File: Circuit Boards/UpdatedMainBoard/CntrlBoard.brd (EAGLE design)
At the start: 101.6 x 81.3 mm, 49 parts, among them P1 22-23-2021, P10 3PIN2MMPITCH, P11 3PIN2MMPITCH, P12 DF3A-2P-2DSA, P13 DF3A-2P-2DSA, P14 DF3A-2P-2DSA, P15 DF3A-2P-2DSA, P16 DF3A-2P-2DSA, P17 DF3A-2P-2DSA, P18 DF3A-2P-2DSA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

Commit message: Control Board update finished
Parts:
- added R13: 100R, resistor:R1206
- added R14: 300R, resistor:R1206
- added U$3: RSHUNT, resistor:CM2512SHUNT
- added U$4: LT6106, linear-technology:TSOT23-6
- P10, P11, P7, P8, P9: value 3PIN2MMPITCH -> 3MM2MMLOCKING; device con-3m:3PIN_2MMPITCH -> con-3m:3PIN_2MMLOCKING
- moved LED3 94.6 mm to (98.4, 18.4), turned to 0 degrees
- moved P7 14.7 mm to (51.4, 14.0)
- moved P8 10.9 mm to (57.8, 14.0)
- moved U$1 8.91 mm to (61.0, 4.45)
- moved R9 8.26 mm to (3.81, 73.0), turned to 90 degrees
- moved P9 7.10 mm to (64.1, 14.0)
- moved R8 6.38 mm to (3.17, 66.0)
- moved P14 6.35 mm to (6.35, 50.8)
- moved LED4 4.49 mm to (12.1, 66.7)
- moved P16 4.45 mm to (6.35, 45.1)
- moved P2 3.81 mm to (8.89, 15.2)
- moved P10 3.42 mm to (70.5, 14.0)
- moved P12 3.17 mm to (14.0, 42.5)
- moved P13 2.54 mm to (14.0, 50.8)
- moved P15 2.54 mm to (6.35, 39.4)
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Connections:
- new net N$22: SW1.1, U$3.I2
- new net N$24: R13.1, U$3.E2
- new net N$25: R13.2, U$4.3
- new net N$26: U$3.E1, U$4.4
- new net V_CURRENT: R14.1, U$4.1, U1.A7
- net GND: now also R14.2, U$4.2
- net VCC: now also U$3.I1, U$4.6; no longer SW1.1
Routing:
- net N$12: track 7.01 -> 144.8 mm, vias 1 -> 3
- net VCC: track 175.4 -> 240.4 mm, vias 5 -> 8
- net N$25: track 0.00 -> 54.2 mm, vias 0 -> 1
- net GND: track 454.3 -> 488.3 mm, vias 5 -> 7
- net N$26: track 0.00 -> 32.2 mm, vias 0 -> 1
- net V_CURRENT: track 0.00 -> 26.2 mm
- net N$22: track 0.00 -> 17.9 mm
- net +5V: track 191.9 -> 208.4 mm
- net TANK_LEVEL: track 14.5 -> 27.8 mm
- net N$27: track 28.2 -> 37.9 mm
- net N$1: track 67.2 -> 57.7 mm
- net LIN_POS: track 14.5 -> 24.0 mm
- net N$24: track 0.00 -> 9.12 mm
- net ROT_POS: track 14.5 -> 20.2 mm
- net N$10: track 8.26 -> 11.4 mm
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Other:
- outline, holes or cut-outs redrawn
- board text added: "24V"
- board text added: "24V IN"
- board text added: "24V OUT"
- board text added: "24V OUTS"
- board text added: "5V"
- board text added: "5V ENABLE"
- board text added: "5V OUT"
- board text added: "5V OUTS"
- board text added: "IMU SERIAL"
- board text added: "LINEAR"
- board text added: "PUMP DIR."
- board text added: "PUMP DIRECTION"
- board text added: "PUMP ON"
- board text added: "ROTARY"

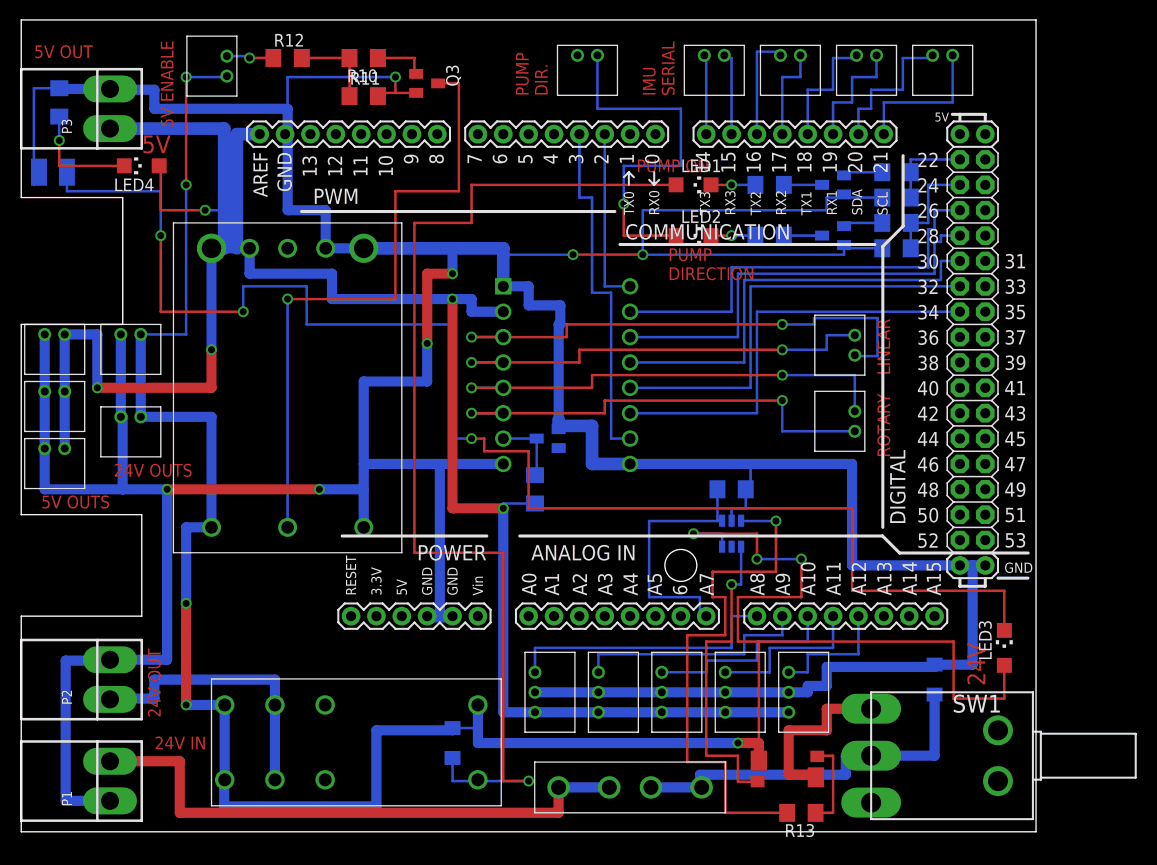
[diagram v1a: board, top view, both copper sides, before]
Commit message: Added 6 pin connector
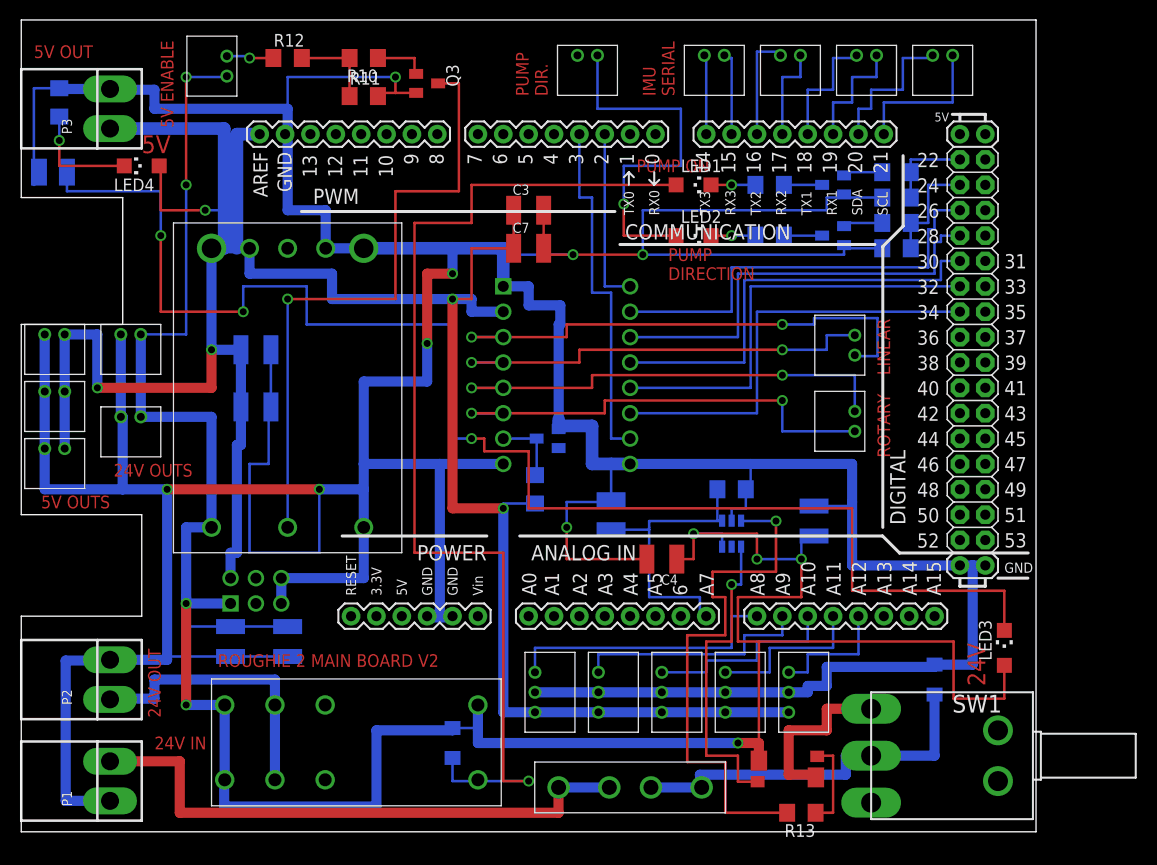
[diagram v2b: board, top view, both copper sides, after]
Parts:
- added C1, C2, C3, C4: 10U, resistor:C1210K
- added C5, C6, C7, C8, C9: 0U1, resistor:C1210K
- added P22: 6PIN2ROWARDUINO, con-3m:6PIN2ROWARDUINO
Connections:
- net +5V: now also C1.1, C3.1, C6.1, C7.1, P22.P$2
- net GND: now also C1.2, C2.2, C3.2, C4.2, C5.2, C6.2, C7.2, C8.2, C9.2, P22.P$5, P22.P$6
- net VCC: now also C2.1, C4.1, C5.1, C8.1, P22.P$1
- net V_CURRENT: now also C9.1
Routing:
- net GND: track 488.3 -> 585.7 mm, vias 7 -> 8
- net +5V: track 208.4 -> 250.3 mm
- net VCC: track 240.4 -> 265.4 mm
- net V_CURRENT: track 26.2 -> 30.0 mm
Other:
- board text added: "ROUGHIE 2 MAIN BOARD V2"
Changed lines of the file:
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@@
 DIR.</text>
 <text x="15.24" y="70.485" size="1.27" layer="1" font="vector" rot="R90">5V ENABLE</text>
+<text x="19.685" y="16.51" size="1.27" layer="1" font="vector">ROUGHIE 2 MAIN BOARD V2</text>
 </plain>
 <attributes>
@@
 <element name="U$4" library="linear-technology" package="TSOT23-6" value="LT6106" x="71.12" y="29.845" rot="MR180"/>
 <element name="R14" library="resistor" package="R1206" value="300R" x="71.12" y="34.29" rot="MR180"/>
+<element name="C1" library="resistor" package="C1210K" value="10U" x="23.495" y="48.26" rot="MR180"/>
+<element name="C2" library="resistor" package="C1210K" value="10U" x="20.955" y="19.05" rot="MR270"/>
+<element name="C3" library="resistor" package="C1210K" value="10U" x="50.8" y="62.23"/>
+<element name="C4" library="resistor" package="C1210K" value="10U" x="64.135" y="27.305" rot="R180"/>
+<element name="C5" library="resistor" package="C1210K" value="0U1" x="26.67" y="19.05" rot="MR270"/>
+<element name="C6" library="resistor" package="C1210K" value="0U1" x="23.495" y="42.545" rot="MR180"/>
+<element name="C7" library="resistor" package="C1210K" value="0U1" x="50.8" y="58.42"/>
+<element name="C8" library="resistor" package="C1210K" value="0U1" x="79.375" y="31.115" rot="MR90"/>
+<element name="C9" library="resistor" package="C1210K" value="0U1" x="59.055" y="31.75" rot="MR90"/>
+<element name="P22" library="con-3m" package="6PIN2ROWARDUINO" value="6PIN2ROWARDUINO" x="20.955" y="22.86"/>
 </elements>
 <signals>
@@
 <wire x1="60.96" y1="36.83" x2="73.025" y2="36.83" width="1.016" layer="16"/>
 <wire x1="73.025" y1="36.83" x2="83.185" y2="36.83" width="1.016" layer="16"/>
-<wire x1="83.185" y1="36.83" x2="83.185" y2="26.67" width="1.016" layer="16"/>
+<wire x1="83.185" y1="36.83" x2="83.185" y2="33.02" width="1.016" layer="16"/>
+<wire x1="83.185" y1="33.02" x2="83.185" y2="26.67" width="1.016" layer="16"/>
 <wire x1="83.185" y1="26.67" x2="93.98" y2="26.67" width="1.016" layer="16"/>
 <wire x1="48.26" y1="54.61" x2="50.8" y2="54.61" width="1.016" layer="16"/>
@@
 <wire x1="40.64" y1="21.59" x2="41.91" y2="21.59" width="1.016" layer="16"/>
 <wire x1="41.91" y1="21.59" x2="41.91" y2="36.83" width="1.016" layer="16"/>
-<wire x1="60.96" y1="36.83" x2="57.15" y2="36.83" width="1.27" layer="16"/>
+<wire x1="60.96" y1="36.83" x2="59.055" y2="36.83" width="1.27" layer="16"/>
+<wire x1="59.055" y1="36.83" x2="57.15" y2="36.83" width="1.27" layer="16"/>
 <wire x1="57.15" y1="36.83" x2="57.15" y2="40.64" width="1.27" layer="16"/>
 <wire x1="57.15" y1="40.64" x2="53.805" y2="40.64" width="1.27" layer="16"/>
@@
 <wire x1="2.350009375" y1="34.29" x2="2.350009375" y2="38.369240625" width="1.016" layer="16"/>
 <wire x1="9.970009375" y1="49.799240625" x2="9.970009375" y2="41.544240625" width="1.016" layer="16"/>
-<wire x1="14.605" y1="17.2212" x2="14.605" y2="34.29" width="1.016" layer="16"/>
+<wire x1="14.605" y1="17.2212" x2="14.605" y2="17.55" width="1.016" layer="16"/>
 <via x="14.605" y="34.29" extent="1-16" drill="0.7" shape="square"/>
+<wire x1="14.605" y1="17.55" x2="14.605" y2="34.29" width="1.016" layer="16"/>
 <wire x1="14.605" y1="34.29" x2="29.845" y2="34.29" width="1.016" layer="1"/>
 <via x="29.845" y="34.29" extent="1-16" drill="0.7" shape="square"/>
@@
 <wire x1="71.12" y1="32.385" x2="72.542" y2="32.385" width="0.254" layer="16"/>
 <wire x1="72.542" y1="32.385" x2="72.542" y2="34.29" width="0.254" layer="16"/>
+<contactref element="C4" pad="2"/>
+<contactref element="C8" pad="2"/>
+<contactref element="C9" pad="2"/>
+<contactref element="C3" pad="2"/>
+<contactref element="C7" pad="2"/>
+<contactref element="C2" pad="2"/>
+<contactref element="C5" pad="2"/>
+<contactref element="C1" pad="2"/>
+<contactref element="C6" pad="2"/>
+<wire x1="59.055" y1="33.25" x2="59.055" y2="36.83" width="0.254" layer="16"/>
+<wire x1="62.635" y1="27.305" x2="54.61" y2="27.305" width="0.254" layer="1"/>
+<wire x1="54.61" y1="27.305" x2="54.61" y2="30.48" width="0.254" layer="1"/>
+<via x="54.61" y="30.48" extent="1-16" drill="0.7" shape="square"/>
+<wire x1="54.61" y1="30.48" x2="54.61" y2="33.02" width="0.254" layer="16"/>
+<wire x1="54.61" y1="33.02" x2="59.055" y2="33.02" width="0.254" layer="16"/>
+<wire x1="59.055" y1="33.02" x2="59.055" y2="33.25" width="0.254" layer="16"/>
+<wire x1="79.375" y1="32.615" x2="83.185" y2="32.615" width="0.254" layer="16"/>
+<wire x1="83.185" y1="32.615" x2="83.185" y2="33.02" width="0.254" layer="16"/>
+<wire x1="52.3" y1="62.23" x2="52.3" y2="58.42" width="0.254" layer="1"/>
+<wire x1="52.3" y1="58.42" x2="52.705" y2="58.42" width="0.254" layer="1"/>
+<wire x1="52.705" y1="58.42" x2="52.705" y2="57.785" width="0.254" layer="1"/>
+<wire x1="52.705" y1="57.785" x2="55.245" y2="57.785" width="0.254" layer="1"/>
+<wire x1="24.995" y1="48.26" x2="24.995" y2="42.545" width="0.254" layer="16"/>
+<wire x1="24.995" y1="42.545" x2="24.765" y2="42.545" width="0.254" layer="16"/>
+<wire x1="24.765" y1="42.545" x2="24.765" y2="36.83" width="0.254" layer="16"/>
+<wire x1="24.765" y1="36.83" x2="22.86" y2="36.83" width="0.254" layer="16"/>
+<wire x1="22.86" y1="36.83" x2="22.86" y2="27.94" width="0.254" layer="16"/>
+<wire x1="22.86" y1="27.94" x2="29.845" y2="27.94" width="0.254" layer="16"/>
+<wire x1="29.845" y1="27.94" x2="29.845" y2="34.29" width="0.254" layer="16"/>
+<wire x1="26.67" y1="17.55" x2="20.955" y2="17.55" width="0.254" layer="16"/>
+<wire x1="20.955" y1="17.55" x2="14.605" y2="17.55" width="0.254" layer="16"/>
+<contactref element="P22" pad="P$6"/>
+<contactref element="P22" pad="P$5"/>
+<wire x1="26.035" y1="22.86" x2="26.035" y2="25.4" width="1.016" layer="16"/>
+<wire x1="26.035" y1="25.4" x2="34.29" y2="25.4" width="1.016" layer="16"/>
+<wire x1="34.29" y1="25.4" x2="34.29" y2="30.48" width="1.016" layer="16"/>
 </signal>
 <signal name="N$1">
@@
 <wire x1="45.72" y1="10.3886" x2="45.72" y2="10.16" width="0.254" layer="16"/>
 <wire x1="19.05" y1="30.48" x2="16.51" y2="30.48" width="1.016" layer="16"/>
-<wire x1="16.51" y1="30.48" x2="16.51" y2="22.86" width="1.016" layer="16"/>
+<wire x1="16.51" y1="30.48" x2="16.51" y2="23.495" width="1.016" layer="16"/>
 <via x="16.51" y="22.86" extent="1-16" drill="0.7" shape="square"/>
+<wire x1="16.51" y1="23.495" x2="16.51" y2="22.86" width="1.016" layer="16"/>
 <wire x1="16.51" y1="22.86" x2="16.51" y2="12.7" width="1.016" layer="1"/>
 <via x="16.51" y="12.7" extent="1-16" drill="0.7" shape="square"/>
@@
 <wire x1="67.31" y1="29.845" x2="70.17" y2="29.845" width="0.254" layer="16"/>
 <wire x1="70.17" y1="29.845" x2="70.17" y2="28.545" width="0.254" layer="16"/>
+<contactref element="C4" pad="1"/>
+<contactref element="C8" pad="1"/>
+<contactref element="C5" pad="1"/>
+<contactref element="C2" pad="1"/>
+<wire x1="65.635" y1="27.305" x2="67.31" y2="27.305" width="0.254" layer="1"/>
+<wire x1="67.31" y1="27.305" x2="67.31" y2="29.845" width="0.254" layer="1"/>
+<wire x1="79.375" y1="29.615" x2="78.105" y2="29.615" width="0.254" layer="16"/>
+<wire x1="78.105" y1="29.615" x2="78.105" y2="27.305" width="0.254" layer="16"/>
+<wire x1="26.67" y1="20.55" x2="20.955" y2="20.55" width="0.254" layer="16"/>
+<wire x1="16.51" y1="23.725" x2="16.51" y2="23.495" width="0.254" layer="16"/>
+<contactref element="P22" pad="P$1"/>
+<wire x1="20.955" y1="20.55" x2="16.51" y2="20.55" width="0.254" layer="16"/>
+<wire x1="16.51" y1="20.55" x2="16.51" y2="22.86" width="0.254" layer="16"/>
+<wire x1="20.955" y1="22.86" x2="16.51" y2="22.86" width="1.016" layer="16"/>
 </signal>
 <signal name="N$4">
@@
 <wire x1="64.135" y1="11.970003125" x2="70.485" y2="11.970003125" width="1.016" layer="16"/>
 <wire x1="70.485" y1="11.970003125" x2="76.835" y2="11.970003125" width="1.016" layer="16"/>
+<contactref element="C7" pad="1"/>
+<contactref element="C3" pad="1"/>
+<contactref element="C1" pad="1"/>
+<contactref element="C6" pad="1"/>
+<wire x1="49.3" y1="62.23" x2="49.3" y2="58.42" width="0.254" layer="1"/>
+<wire x1="49.3" y1="58.42" x2="45.085" y2="58.42" width="0.254" layer="1"/>
+<wire x1="45.085" y1="58.42" x2="45.085" y2="53.34" width="0.254" layer="1"/>
+<wire x1="45.085" y1="53.34" x2="43.18" y2="53.34" width="0.254" layer="1"/>
+<contactref element="P22" pad="P$2"/>
+<wire x1="21.995" y1="48.26" x2="19.05" y2="48.26" width="1.016" layer="16"/>
+<wire x1="21.995" y1="42.545" x2="21.995" y2="48.26" width="1.016" layer="16"/>
+<wire x1="20.955" y1="25.4" x2="20.955" y2="27.94" width="1.016" layer="16"/>
+<wire x1="20.955" y1="27.94" x2="21.59" y2="27.94" width="1.016" layer="16"/>
+<wire x1="21.59" y1="27.94" x2="21.59" y2="38.735" width="1.016" layer="16"/>
+<wire x1="21.59" y1="38.735" x2="21.995" y2="38.735" width="1.016" layer="16"/>
+<wire x1="21.995" y1="38.735" x2="21.995" y2="42.545" width="1.016" layer="16"/>
 </signal>
 <signal name="N$12">
@@
 <wire x1="67.945" y1="21.59" x2="67.945" y2="23.495" width="0.254" layer="16"/>
 <wire x1="67.945" y1="23.495" x2="62.865" y2="23.495" width="0.254" layer="16"/>
-<wire x1="62.865" y1="23.495" x2="62.865" y2="31.115" width="0.254" layer="16"/>
+<wire x1="62.865" y1="23.495" x2="62.865" y2="30.25" width="0.254" layer="16"/>
+<wire x1="62.865" y1="30.48" x2="62.865" y2="31.115" width="0.254" layer="16"/>
 <wire x1="62.865" y1="31.115" x2="70.17" y2="31.115" width="0.254" layer="16"/>
 <wire x1="70.17" y1="31.115" x2="70.17" y2="31.145" width="0.254" layer="16"/>
+<contactref element="C9" pad="1"/>
+<wire x1="59.055" y1="30.25" x2="62.865" y2="30.25" width="0.254" layer="16"/>
+<wire x1="62.865" y1="30.25" x2="62.865" y2="30.48" width="0.254" layer="16"/>
 </signal>
 <signal name="N$22">
